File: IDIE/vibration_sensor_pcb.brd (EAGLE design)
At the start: 61.3 x 43.4 mm, 63 parts, among them IC1 LORA-E5, IC2 STM32L071KBT6, IC3 FXLS8974CFR3, IC4 FXLS8971CFR1, IC5 DRV5032FBLPGM, IC6 FT234XD-T, J1 217182-0001, Q2 SI2305B-TP, Y1 ABS06-32.768KHZ-9-1-T

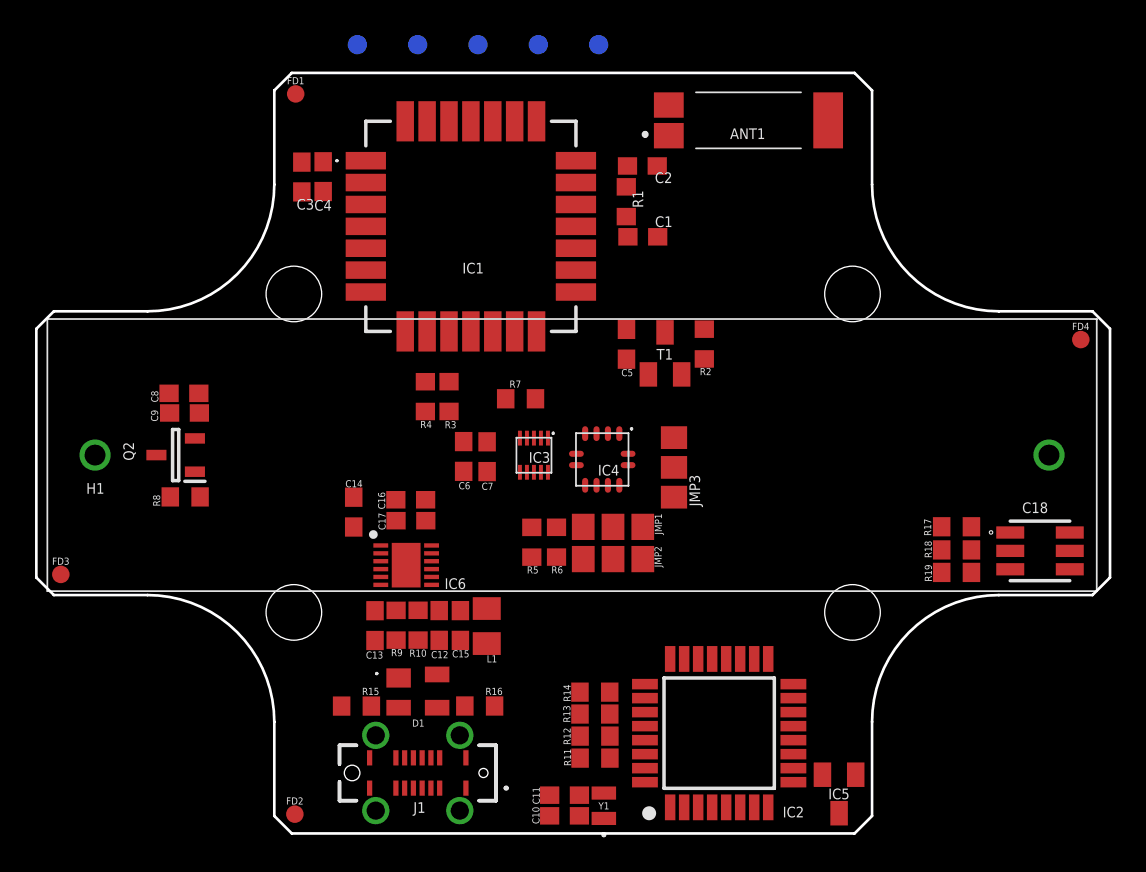
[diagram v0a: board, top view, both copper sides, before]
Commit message: UPDATE orden de pcb y reglas de diseño
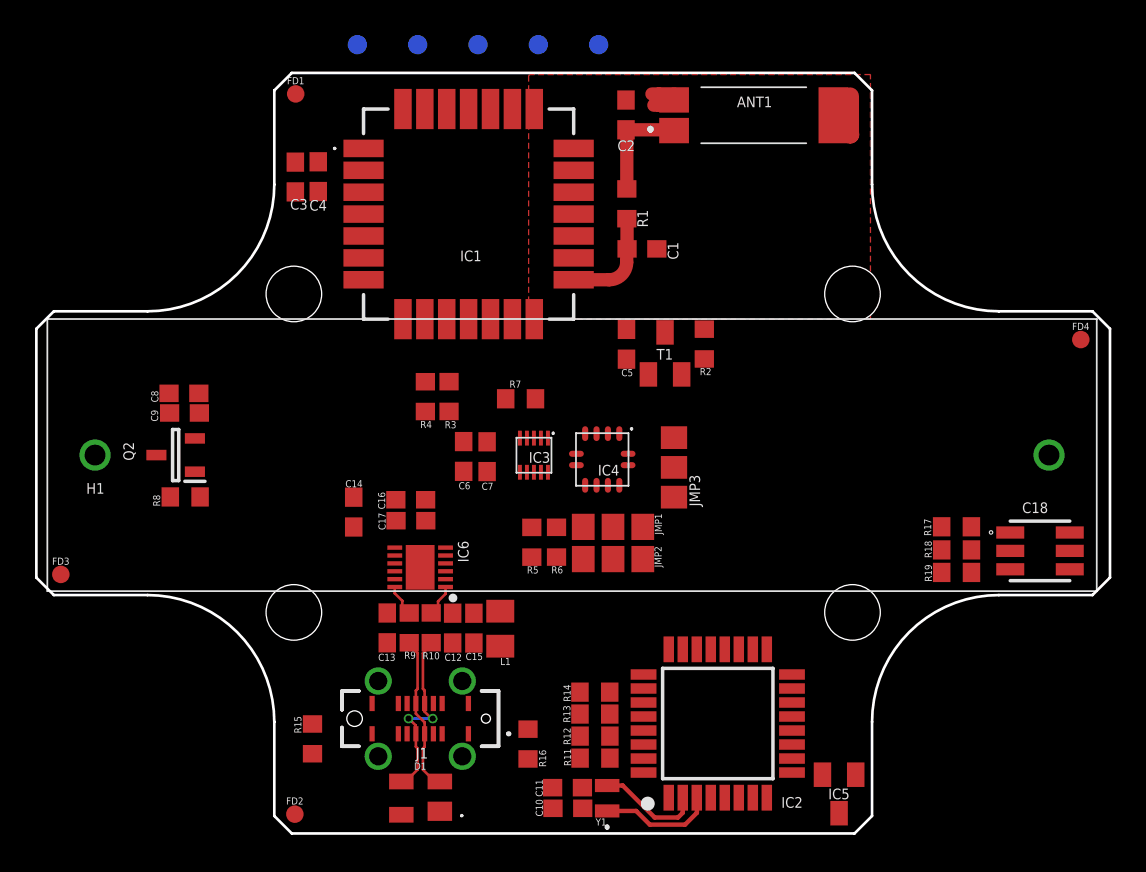
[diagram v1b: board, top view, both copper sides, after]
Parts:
- moved D1 6.12 mm to (22.0, 2.02), turned to 90 degrees
- moved R16 3.51 mm to (28.2, 5.11), turned to 90 degrees
- moved R15 3.13 mm to (15.8, 5.40), turned to 90 degrees
- moved J1 3.11 mm to (22.0, 6.56)
- moved C2 3.06 mm to (33.8, 41.0), turned to 90 degrees
- moved IC6 0.81 mm to (22.0, 15.2), turned to 180 degrees
- moved C12 0.78 mm to (23.9, 11.7)
- moved C15 0.78 mm to (25.1, 11.7)
- moved L1 0.78 mm to (26.6, 11.7)
- moved R10 0.76 mm to (22.6, 11.7)
- moved R9 0.76 mm to (21.4, 11.7)
- moved IC1 0.71 mm to (24.8, 35.4)
- moved C13 0.71 mm to (20.1, 11.7)
- moved C1 0.69 mm to (34.7, 33.4)
- moved IC2 0.56 mm to (39.0, 6.28)
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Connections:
- net GND: now also ANT1.2, ANT1.3
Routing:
- net USB_N: track 0.00 -> 10.5 mm, vias 0 -> 2
- net USB_P: track 0.00 -> 8.98 mm
- net OSC32_OUT: track 0.00 -> 6.59 mm
- net ANT: track 0.00 -> 6.18 mm
- net OSC32_IN: track 0.00 -> 6.04 mm
- net OUT_ANT: track 0.00 -> 5.95 mm
- net GND: track 0.00 -> 3.89 mm
- net USBDM: track 0.00 -> 1.86 mm
- net USBDP: track 0.00 -> 1.82 mm
- added copper zone on layer 1, net GND

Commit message: ADD & UPDATE documentacion, modelado 3d y poco ruteo
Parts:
- moved R8 1.78 mm to (8.40, 17.4)
- moved Q2 1.59 mm to (8.05, 20.0)
- moved C9 1.56 mm to (8.50, 22.5)
- moved C8 1.47 mm to (8.54, 23.7)
- moved H1 0.13 mm to (3.48, 21.7), flipped to the bottom, turned to 180 degrees
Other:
- board text added: "C:/Users/Scort/Downloads/Logotipo-Escuela-Colombiana-de-Ingeniería-Julio-Garavito-1.bmp"
- board text added: "Santiago CT Anthony JG"

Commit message: UPDATE schematic
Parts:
- removed D1: SP0503BAHTG, SamacSys_Parts:SP0503BAHTG
- added IC7: USBLC6-2SC6, SamacSys_Parts:SOT95P280X145-6N
- moved C8 6.65 mm to (14.4, 26.9)
- moved C9 6.65 mm to (14.3, 25.7)
- moved Q2 6.65 mm to (13.9, 23.2)
- moved R8 6.65 mm to (14.2, 20.7)
- moved R7 4.65 mm to (23.2, 26.0)
- moved C6 4.06 mm to (20.4, 21.9)
- moved R4 3.90 mm to (18.4, 25.2)
- moved C7 3.61 mm to (22.2, 21.9)
- moved R3 3.40 mm to (20.3, 25.2)
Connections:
- removed net SCL: JMP2.3
- removed net SDA: JMP1.3
- new net N$10: IC7.3
- new net N$3: IC7.6
- new net N$4: IC7.4
- new net N$7: IC7.1
- net GND: now also IC7.2; no longer D1.1
- net I2C_SCL: now also JMP2.3
- net I2C_SDA: now also JMP1.3
- net USB_N: no longer D1.3
- net USB_P: no longer D1.2
- net VBUS: now also IC7.5; no longer D1.4
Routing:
- net GND: track 3.89 -> 8.15 mm
- net ANT: track 6.18 -> 10.4 mm

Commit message: UPDATE schematic and PCB route
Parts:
- added C19: 1uF, rcl:C0603
- added C20: 0.1uF, rcl:C0603
- added C21: 12.5uF, rcl:C0603
- added JP1: (no value), pinhead:2X03
- added R20, R21: 4.7k, rcl:R0603
- moved TP5 15.9 mm to (23.7, 31.6)
- moved TP4 15.0 mm to (22.2, 31.6)
- moved TP1 10.1 mm to (21.0, 35.2)
- moved IC7 9.59 mm to (21.9, 8.44), turned to 90 degrees
- moved C17 9.49 mm to (29.4, 12.6), turned to 270 degrees
- moved C16 9.28 mm to (28.2, 12.7), turned to 270 degrees
- moved TP2 8.28 mm to (21.1, 36.8)
- moved C14 7.30 mm to (25.2, 16.3), turned to 90 degrees
- moved TP3 6.12 mm to (26.0, 39.0)
- moved R7 5.89 mm to (29.0, 24.7)
- moved C12 3.95 mm to (20.0, 12.5), turned to 90 degrees
- moved C13 3.84 mm to (23.9, 12.5), turned to 90 degrees
- moved R4 3.81 mm to (22.2, 25.7), turned to 270 degrees
- moved C8 3.76 mm to (10.9, 25.4), turned to 180 degrees
- moved C9 3.75 mm to (10.9, 24.1), turned to 180 degrees
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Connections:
- net N$1 renamed INTF_SEL
- net N$9 renamed RESET#
- removed net N$10: IC7.3
- removed net N$3: IC7.6
- removed net N$4: IC7.4
- removed net N$7: IC7.1
- removed net PA11: IC2.21
- removed net PA12: IC2.22
- removed net PA15: IC2.25
- new net GND1: C20.2
- new net N$2: JP1.2
- new net NRST: JP1.4
- new net USBC_N: IC7.3, J1.A7, J1.B7
- new net USBC_P: IC7.1, J1.A6, J1.B6
- net +3V3: now also C19.1, C20.1, JP1.1, R20.2, R21.2
- net BOOT: now also C21.1, IC2.4
- net GND: now also C19.2, C21.2, IC2.31, JP1.6
- net I2C_SCL: now also R21.1
- net I2C_SDA: now also R20.1
- net INT1: now also IC2.22
- net INT2: now also IC2.25
- net MCU_SWCLK: now also JP1.5
- net MCU_SWDIO: now also JP1.3
- net MD_RST: now also IC2.21
- net USB_N: now also IC7.4; no longer J1.A7, J1.B7
- net USB_P: now also IC7.6; no longer J1.A6, J1.B6
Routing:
- net +3V3: track 0.00 -> 126.3 mm
- net SPI_MISO: track 0.00 -> 32.1 mm, vias 0 -> 3
- net SPI_CS: track 0.00 -> 27.5 mm, vias 0 -> 3
- net VBUS: track 0.00 -> 21.0 mm
- net SPI_MOSI: track 0.00 -> 20.1 mm, vias 0 -> 2
- net INT1: track 0.00 -> 19.7 mm
- net INT2: track 0.00 -> 19.5 mm
- net LED_R: track 0.00 -> 17.6 mm, vias 0 -> 2
- net E5_RST: track 0.00 -> 17.5 mm, vias 0 -> 2
- net SPI_SCLK: track 0.00 -> 16.8 mm, vias 0 -> 2
- net SCL/SCLK: track 0.00 -> 16.4 mm, vias 0 -> 3
- net SDA/MOSI: track 0.00 -> 13.2 mm, vias 0 -> 2
- net LED_G: track 0.00 -> 13.2 mm
- net LED_B: track 0.00 -> 12.1 mm
- net RESET#: track 0.00 -> 9.91 mm, vias 0 -> 2
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- added copper zone on layer 1, net +3V3
- added copper zone on layer 16, net GND

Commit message: UPDATE pcb schematic
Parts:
- removed TP1, TP2, TP3, TP4, TP5: PTR1TP11R, testpad:TP11R
- removed Y1: ABS06-32.768KHZ-9-1-T, SamacSys_Parts:ABS06
- added BOOT, INT1, INT2, MCU_RXD, MCU_TXD, SCL/SCLK, SDA/MOSI, SPI_CS, SPI_MISO, SWCLK, SWDIO: PTR1TP11R, testpad:TP11R
- added CRISTAL: CRISTAL-32.768KHZ-9-1-T, SamacSys_Parts:CRISTAL-32.768
- moved R16 12.4 mm to (15.8, 3.67), turned to 270 degrees
- moved C21 4.42 mm to (48.6, 20.9), turned to 270 degrees
- moved C15 3.00 mm to (26.5, 9.77), turned to 0 degrees
- moved R15 1.20 mm to (15.7, 6.59)
- moved C17 0.71 mm to (30.1, 12.5)
- moved C12 0.70 mm to (19.3, 12.5)
- moved C13 0.60 mm to (24.5, 12.5)
- moved JMP2 0.40 mm to (36.1, 15.6)
- moved C16 0.32 mm to (28.5, 12.6)
- moved C6 0.30 mm to (22.0, 21.7)
- moved R9 0.20 mm to (21.1, 12.4)
- moved R17 0.20 mm to (52.0, 14.9)
- moved R19 0.20 mm to (52.0, 17.9)
- moved R4 0.20 mm to (22.0, 25.7)
- moved C5 0.10 mm to (34.4, 28.6)
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- renumbered C18 to RGB, J1 to USB-C, Q2 to MOSFET, T1 to TRANSISTOR
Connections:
- net N$6 renamed GATE
- net BOOT: now also BOOT.TP; no longer C21.1, IC2.4, TP3.TP
- net INT1: now also INT1.TP
- net INT2: now also INT2.TP
- net LORA_RXD: now also MCU_RXD.TP; no longer TP5.TP
- net LORA_TXD: now also MCU_TXD.TP; no longer TP4.TP
- net NRST: now also C21.1, IC2.4
- net OSC32_IN: now also CRISTAL.2; no longer Y1.2
- net OSC32_OUT: now also CRISTAL.1; no longer Y1.1
- net SCL/SCLK: now also SCL/SCLK.TP
- net SDA/MOSI: now also SDA/MOSI.TP
- net SPI_CS: now also SPI_CS.TP
- net SPI_MISO: now also SPI_MISO.TP
- net SWCLK: now also SWCLK.TP; no longer TP1.TP
- net SWDIO: now also SWDIO.TP; no longer TP2.TP
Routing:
- net MCU_TXD: track 0.00 -> 38.0 mm, vias 0 -> 2
- net MCU_RXD: track 0.00 -> 34.3 mm, vias 0 -> 2
- net NRST: track 0.00 -> 31.1 mm, vias 0 -> 2
- net R12: track 0.00 -> 24.3 mm, vias 0 -> 2
- net R14: track 0.00 -> 23.7 mm, vias 0 -> 2
- net R13: track 0.00 -> 21.9 mm, vias 0 -> 2
- net R11: track 0.00 -> 21.0 mm, vias 0 -> 2
- net MCU_SWDIO: track 0.00 -> 20.7 mm, vias 0 -> 1
- net MCU_SWCLK: track 0.00 -> 19.5 mm, vias 0 -> 1
- net MD_RST: track 0.00 -> 19.0 mm, vias 0 -> 2
- net SDA/MOSI: track 13.2 -> 28.3 mm
- net SCL/SCLK: track 16.4 -> 30.7 mm
- net SPI_MISO: track 32.1 -> 41.6 mm
- net A5: track 0.00 -> 8.12 mm, vias 0 -> 2
- net B5: track 0.00 -> 7.55 mm
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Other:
- board text added: "+3V3"
- board text added: "GND"
- board text added: "NRST"
- board text added: "OH NO"
- board text added: "SWCLK"
- board text added: "SWDIO"
- board text added: "X"
